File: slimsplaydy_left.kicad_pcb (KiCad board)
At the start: 2 copper layers, 122.6 x 97.5 mm, 37 parts

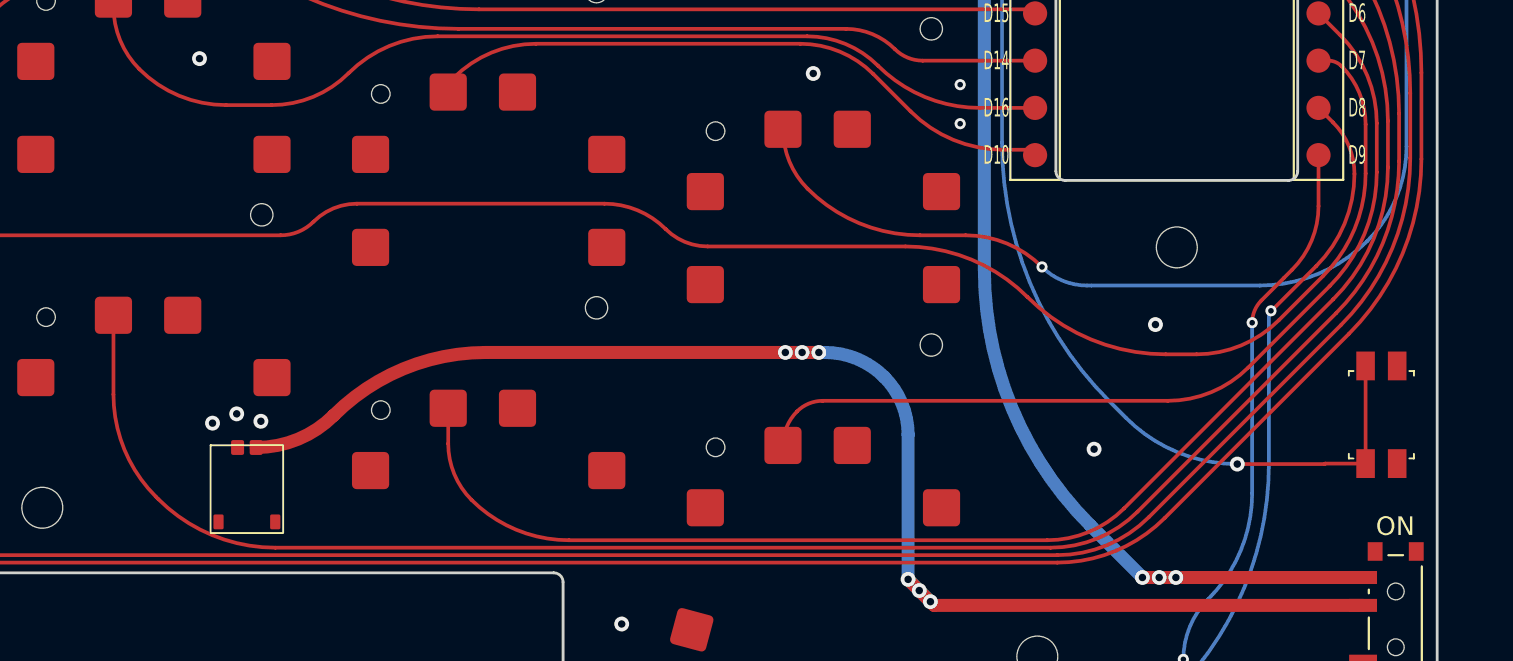
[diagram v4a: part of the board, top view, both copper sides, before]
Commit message: Cleanup ergogen and other from ezmate 1.0mm -> 1.2mm swap
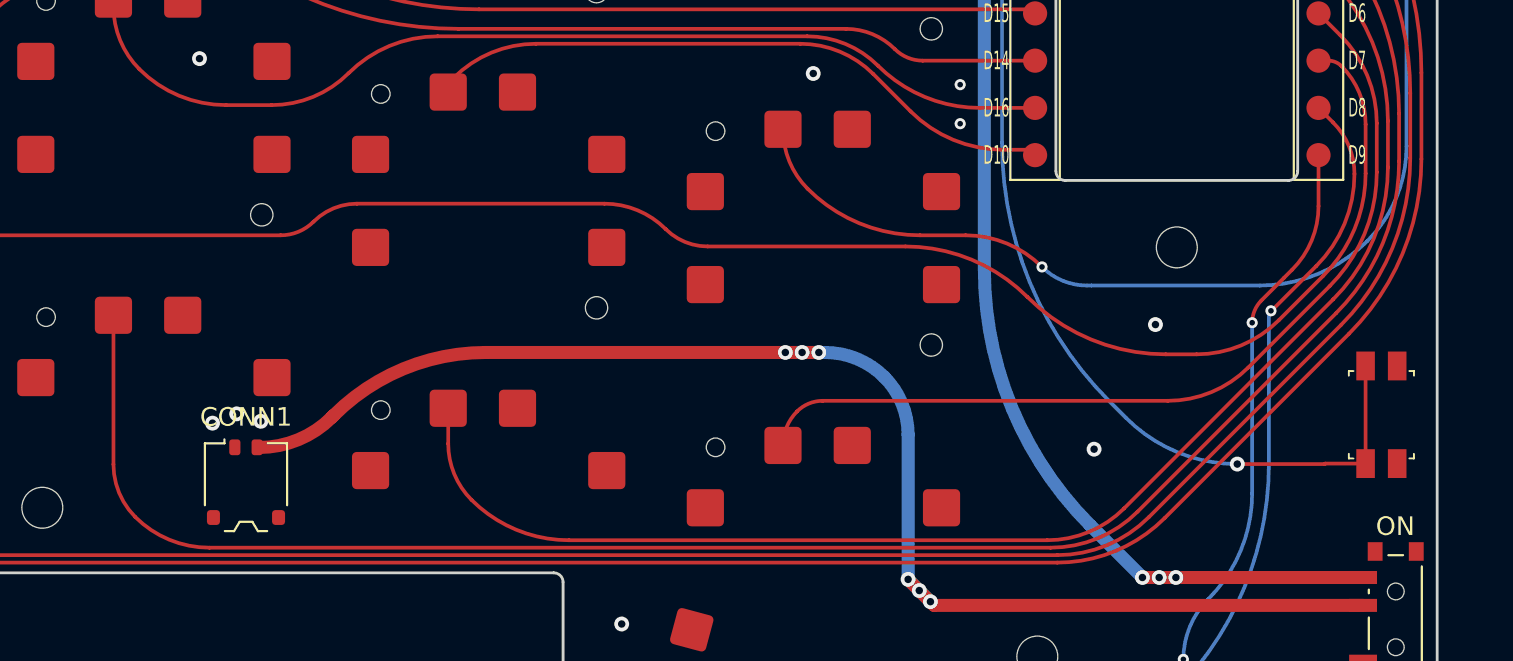
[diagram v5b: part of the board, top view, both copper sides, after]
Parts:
- CONN1: footprint Molex_Pico_EZMate_Plus_1x02 -> Connector_Molex:Molex_Pico-EZmate_78171-0002_1x02-1MP_P1.20mm_Vertical
- moved CONN1 0.38 mm to (40.0, -8.82)
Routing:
- net finger_middle_bottom: track 102.5 -> 104.2 mm
